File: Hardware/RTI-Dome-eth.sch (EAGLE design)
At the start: 79 parts, among them IC1 24AA128ST, IC3 FT232RL, IC5 74LVC245, IC6 74ABT245, J1 POWERPOLE_POWER45A, U1 W5500, X13 PN61729-S, X9 J1011F21PNL

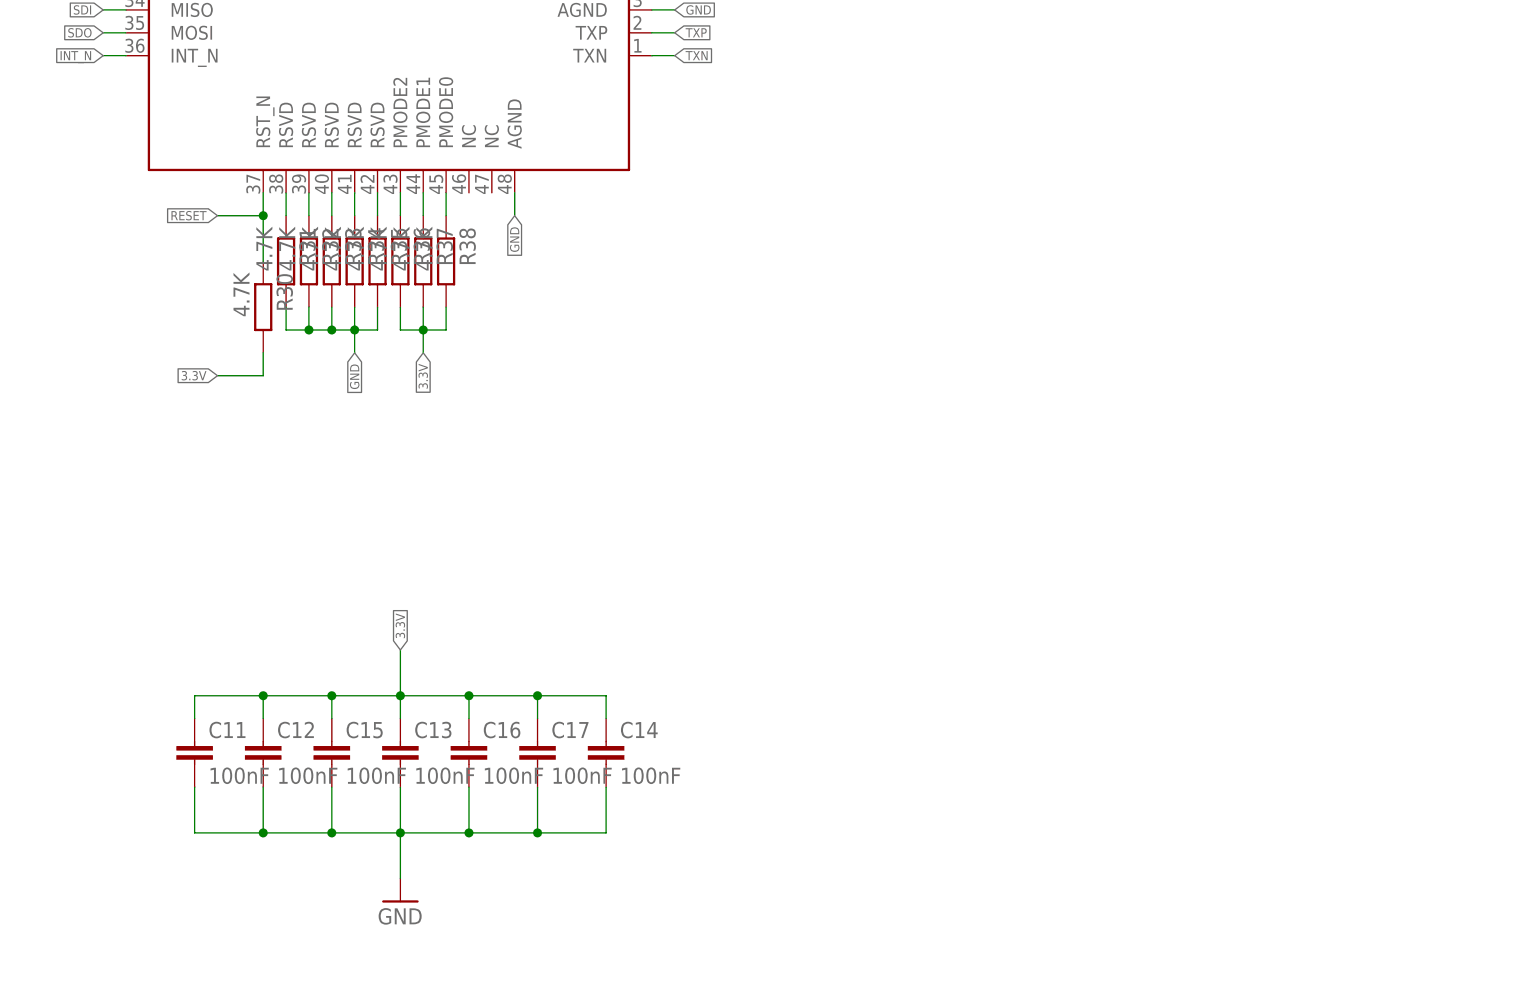
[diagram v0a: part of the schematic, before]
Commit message: Started routing the W5500
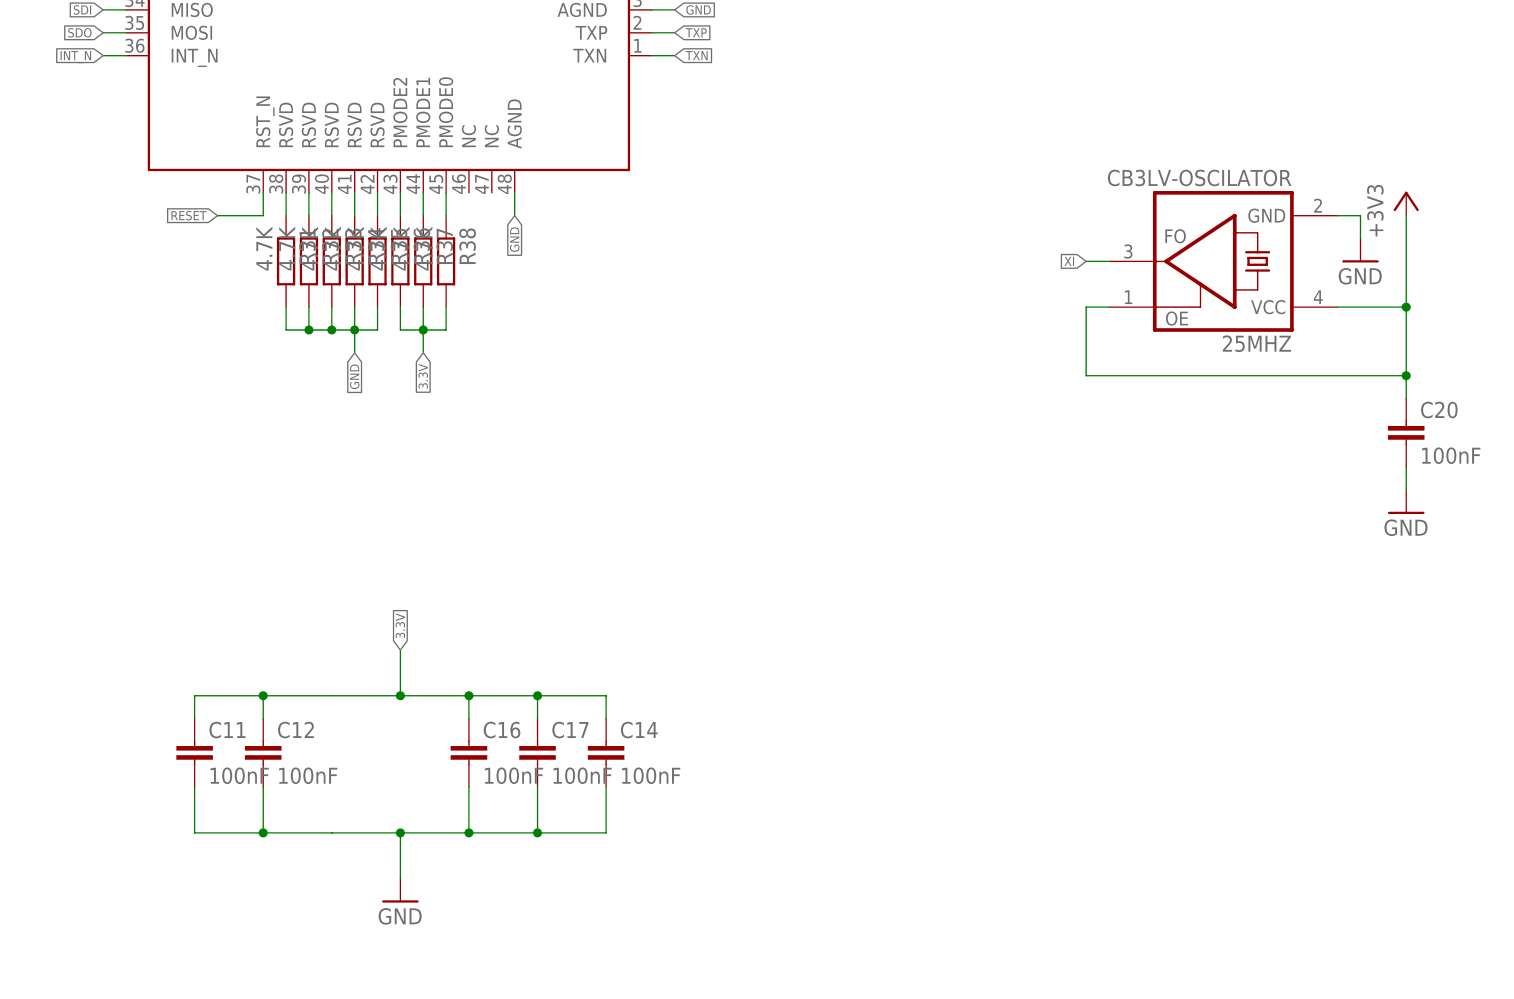
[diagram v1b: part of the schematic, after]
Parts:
- removed C13, C15: 100nF, rti:C-EU'0805'
- removed R30: 4.7K, rti:R-EU'0805'
- added 25MHZ: CB3LV-OSCILATOR, rti:CB3LV-OSCILATOR
- added C20: 100nF, rti:C-EU'0805'
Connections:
- new net +3V3: 25MHZ.OE, 25MHZ.VDD, C20.1
- net 3.3V: no longer C13.1, C15.1, R30.2
- net GND: now also 25MHZ.GND, C20.2; no longer C13.2, C15.2
- net RESET: no longer R30.1
- net XI: now also 25MHZ.FO
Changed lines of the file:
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@@
 <part name="X9" library="rti" deviceset="J1011F" device="" technology="21PNL" value="J1011F21PNL"/>
 <part name="GND16" library="supply1" deviceset="GND" device=""/>
-<part name="R30" library="rti" deviceset="R-EU" device="'0805'" value="4.7K"/>
 <part name="R31" library="rti" deviceset="R-EU" device="'0805'" value="4.7K"/>
 <part name="R32" library="rti" deviceset="R-EU" device="'0805'" value="4.7K"/>
@@
 <part name="C11" library="rti" deviceset="C-EU" device="'0805'" value="100nF"/>
 <part name="C12" library="rti" deviceset="C-EU" device="'0805'" value="100nF"/>
-<part name="C13" library="rti" deviceset="C-EU" device="'0805'" value="100nF"/>
 <part name="C14" library="rti" deviceset="C-EU" device="'0805'" value="100nF"/>
-<part name="C15" library="rti" deviceset="C-EU" device="'0805'" value="100nF"/>
 <part name="C16" library="rti" deviceset="C-EU" device="'0805'" value="100nF"/>
 <part name="C17" library="rti" deviceset="C-EU" device="'0805'" value="100nF"/>
@@
 <part name="R40" library="rti" deviceset="R-EU" device="'0805'" value="4.7K"/>
 <part name="J1" library="powerpoles" deviceset="POWERPOLE_POWER" device="45A"/>
+<part name="GND15" library="supply1" deviceset="GND" device=""/>
+<part name="25MHZ" library="rti" deviceset="CB3LV-OSCILATOR" device=""/>
+<part name="+3V15" library="supply1" deviceset="+3V3" device=""/>
+<part name="C20" library="rti" deviceset="C-EU" device="'0805'" value="100nF"/>
+<part name="GND17" library="supply1" deviceset="GND" device=""/>
 </parts>
 <sheets>
@@
 <instance part="X9" gate="G$1" x="568.96" y="269.24"/>
 <instance part="GND16" gate="1" x="548.64" y="233.68"/>
-<instance part="R30" gate="G$1" x="469.9" y="127" rot="R270"/>
 <instance part="R31" gate="G$1" x="472.44" y="132.08" rot="R270"/>
 <instance part="R32" gate="G$1" x="474.98" y="132.08" rot="R270"/>
@@
 <instance part="C11" gate="G$1" x="462.28" y="78.74"/>
 <instance part="C12" gate="G$1" x="469.9" y="78.74"/>
-<instance part="C13" gate="G$1" x="485.14" y="78.74"/>
 <instance part="C14" gate="G$1" x="508" y="78.74"/>
-<instance part="C15" gate="G$1" x="477.52" y="78.74"/>
 <instance part="C16" gate="G$1" x="492.76" y="78.74"/>
 <instance part="C17" gate="G$1" x="500.38" y="78.74"/>
@@
 <instance part="R40" gate="G$1" x="472.44" y="205.74" rot="R270"/>
 <instance part="J1" gate="G$1" x="378.46" y="83.82"/>
+<instance part="GND15" gate="1" x="591.82" y="132.08"/>
+<instance part="25MHZ" gate="G$1" x="576.58" y="132.08" rot="R180"/>
+<instance part="+3V15" gate="G$1" x="596.9" y="139.7"/>
+<instance part="C20" gate="G$1" x="596.9" y="114.3"/>
+<instance part="GND17" gate="1" x="596.9" y="104.14"/>
 </instances>
 <busses>
@@
 <wire x1="492.76" y1="73.66" x2="492.76" y2="68.58" width="0.1524" layer="91"/>
 <junction x="492.76" y="68.58"/>
-<pinref part="C13" gate="G$1" pin="2"/>
-<wire x1="485.14" y1="73.66" x2="485.14" y2="68.58" width="0.1524" layer="91"/>
 <junction x="485.14" y="68.58"/>
-<pinref part="C15" gate="G$1" pin="2"/>
-<wire x1="477.52" y1="73.66" x2="477.52" y2="68.58" width="0.1524" layer="91"/>
-<junction x="477.52" y="68.58"/>
 <pinref part="C12" gate="G$1" pin="2"/>
 <wire x1="469.9" y1="73.66" x2="469.9" y2="68.58" width="0.1524" layer="91"/>
@@
 <wire x1="472.44" y1="213.36" x2="472.44" y2="210.82" width="0.1524" layer="91"/>
 <label x="469.9" y="213.36" size="1.016" layer="95" rot="R180" xref="yes"/>
+</segment>
+<segment>
+<wire x1="589.28" y1="137.16" x2="591.82" y2="137.16" width="0.1524" layer="91"/>
+<wire x1="591.82" y1="137.16" x2="591.82" y2="134.62" width="0.1524" layer="91"/>
+<pinref part="GND15" gate="1" pin="GND"/>
+<pinref part="25MHZ" gate="G$1" pin="GND"/>
+</segment>
+<segment>
+<pinref part="C20" gate="G$1" pin="2"/>
+<wire x1="596.9" y1="106.68" x2="596.9" y2="109.22" width="0.1524" layer="91"/>
+<pinref part="GND17" gate="1" pin="GND"/>
 </segment>
 </net>
@@
 <wire x1="469.9" y1="81.28" x2="469.9" y2="83.82" width="0.1524" layer="91"/>
 <junction x="469.9" y="83.82"/>
-<pinref part="C15" gate="G$1" pin="1"/>
-<wire x1="477.52" y1="81.28" x2="477.52" y2="83.82" width="0.1524" layer="91"/>
-<junction x="477.52" y="83.82"/>
-<pinref part="C13" gate="G$1" pin="1"/>
-<wire x1="485.14" y1="81.28" x2="485.14" y2="83.82" width="0.1524" layer="91"/>
 <junction x="485.14" y="83.82"/>
 <pinref part="C16" gate="G$1" pin="1"/>
@@
 <wire x1="487.68" y1="124.46" x2="487.68" y2="121.92" width="0.1524" layer="91"/>
 <label x="487.68" y="121.92" size="1.016" layer="95" rot="R270" xref="yes"/>
-</segment>
-<segment>
-<pinref part="R30" gate="G$1" pin="2"/>
-<wire x1="469.9" y1="121.92" x2="469.9" y2="119.38" width="0.1524" layer="91"/>
-<wire x1="469.9" y1="119.38" x2="464.82" y2="119.38" width="0.1524" layer="91"/>
-<label x="464.82" y="119.38" size="1.016" layer="95" rot="R180" xref="yes"/>
 </segment>
 </net>
@@
 <label x="452.12" y="170.18" size="1.016" layer="95" rot="R180" xref="yes"/>
 </segment>
+<segment>
+<wire x1="563.88" y1="132.08" x2="561.34" y2="132.08" width="0.1524" layer="91"/>
+<pinref part="25MHZ" gate="G$1" pin="FO"/>
+<label x="561.34" y="132.08" size="1.016" layer="95" rot="R180" xref="yes"/>
+</segment>
 </net>
 <net name="XO" class="0">
@@
 <segment>
 <pinref part="U1" gate="G$1" pin="RST_N"/>
-<wire x1="469.9" y1="132.08" x2="469.9" y2="137.16" width="0.1524" layer="91"/>
-<pinref part="R30" gate="G$1" pin="1"/>
 <wire x1="469.9" y1="137.16" x2="469.9" y2="139.7" width="0.1524" layer="91"/>
 <wire x1="469.9" y1="137.16" x2="464.82" y2="137.16" width="0.1524" layer="91"/>
-<junction x="469.9" y="137.16"/>
 <label x="464.82" y="137.16" size="1.016" layer="95" rot="R180" xref="yes"/>
 </segment>
@@
 </segment>
 </net>
+<net name="+3V3" class="3">
+<segment>
+<wire x1="589.28" y1="127" x2="596.9" y2="127" width="0.1524" layer="91"/>
+<wire x1="596.9" y1="127" x2="596.9" y2="137.16" width="0.1524" layer="91"/>
+<wire x1="596.9" y1="119.38" x2="596.9" y2="127" width="0.1524" layer="91"/>
+<junction x="596.9" y="127"/>
+<pinref part="+3V15" gate="G$1" pin="+3V3"/>
+<pinref part="25MHZ" gate="G$1" pin="VDD"/>
+<pinref part="25MHZ" gate="G$1" pin="OE"/>
+<wire x1="563.88" y1="127" x2="561.34" y2="127" width="0.1524" layer="91"/>
+<wire x1="561.34" y1="127" x2="561.34" y2="119.38" width="0.1524" layer="91"/>
+<wire x1="561.34" y1="119.38" x2="596.9" y2="119.38" width="0.1524" layer="91"/>
+<pinref part="C20" gate="G$1" pin="1"/>
+<wire x1="596.9" y1="119.38" x2="596.9" y2="116.84" width="0.1524" layer="91"/>
+<junction x="596.9" y="119.38"/>
+</segment>
+</net>

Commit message: Added proper ethernet chip reset.
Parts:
- removed X12: (no value), con-ptr500:AK500/2
- added R30: 4.7K, rti:R-EU'0805'
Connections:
- removed net +3V3: 25MHZ.OE, 25MHZ.VDD, C20.1
- removed net RESET: U$1.RESET., U1.RST_N
- new net ETH_RESET: R30.1, U$1.53, U1.RST_N
- net 3.3V: now also 25MHZ.OE, 25MHZ.VDD, C20.1, R30.2
- net GND: now also U$1.GND@2, U$1.GND@3, U$1.GND@4, U$1.GND@5, U$1.GND@6; no longer U$1.GND., U$1.GND.., U$1.GND..., U$1.GND...., U$1.GND__, X12-1.KL, X12-2.KL
- net INT_N: now also U$1.32
- net VCC: now also U$1.+5V@3, U$1.+5V@4; no longer U$1.+5V., U$1.+5V..
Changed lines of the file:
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@@
 <part name="R3" library="rti" deviceset="R-EU" device="'0805'" value="1K"/>
 <part name="C5" library="rti" deviceset="C-EU" device="'0805'" value="100nF"/>
-<part name="X12" library="con-ptr500" deviceset="AK500/2" device=""/>
 <part name="IC3" library="ftdichip" deviceset="FT232R" device="L"/>
 <part name="GND10" library="supply1" deviceset="GND" device=""/>
@@
 <part name="GND15" library="supply1" deviceset="GND" device=""/>
 <part name="25MHZ" library="rti" deviceset="CB3LV-OSCILATOR" device=""/>
-<part name="+3V15" library="supply1" deviceset="+3V3" device=""/>
 <part name="C20" library="rti" deviceset="C-EU" device="'0805'" value="100nF"/>
 <part name="GND17" library="supply1" deviceset="GND" device=""/>
+<part name="R30" library="rti" deviceset="R-EU" device="'0805'" value="4.7K"/>
 </parts>
 <sheets>
@@
 <instance part="R3" gate="G$1" x="40.64" y="248.92" rot="R90"/>
 <instance part="C5" gate="G$1" x="114.3" y="180.34"/>
-<instance part="X12" gate="-1" x="378.46" y="129.54" rot="R180"/>
-<instance part="X12" gate="-2" x="378.46" y="134.62" rot="R180"/>
 <instance part="IC3" gate="1" x="289.56" y="149.86"/>
 <instance part="GND10" gate="1" x="274.32" y="111.76"/>
@@
 <instance part="GND15" gate="1" x="591.82" y="132.08"/>
 <instance part="25MHZ" gate="G$1" x="576.58" y="132.08" rot="R180"/>
-<instance part="+3V15" gate="G$1" x="596.9" y="139.7"/>
 <instance part="C20" gate="G$1" x="596.9" y="114.3"/>
 <instance part="GND17" gate="1" x="596.9" y="104.14"/>
+<instance part="R30" gate="G$1" x="469.9" y="129.54" rot="R270"/>
 </instances>
 <busses>
@@
 <wire x1="93.98" y1="106.68" x2="93.98" y2="104.14" width="0.1524" layer="91"/>
 <junction x="93.98" y="104.14"/>
-<pinref part="U$1" gate="G$1" pin="GND."/>
-<pinref part="U$1" gate="G$1" pin="GND.."/>
+<pinref part="U$1" gate="G$1" pin="GND@2"/>
+<pinref part="U$1" gate="G$1" pin="GND@3"/>
 </segment>
 <segment>
@@
 </segment>
 <segment>
-<pinref part="X12" gate="-1" pin="KL"/>
-<wire x1="370.84" y1="129.54" x2="373.38" y2="129.54" width="0.1524" layer="91"/>
-<label x="370.84" y="129.54" size="1.016" layer="95" rot="R180" xref="yes"/>
-</segment>
-<segment>
 <wire x1="116.84" y1="243.84" x2="119.38" y2="243.84" width="0.1524" layer="91"/>
 <label x="116.84" y="243.84" size="0.8128" layer="95" rot="R180" xref="yes"/>
@@
 <label x="187.96" y="238.76" size="0.8128" layer="95" rot="R180" xref="yes"/>
 <pinref part="IC6" gate="G$1" pin="A7"/>
-</segment>
-<segment>
-<pinref part="X12" gate="-2" pin="KL"/>
-<wire x1="370.84" y1="134.62" x2="373.38" y2="134.62" width="0.1524" layer="91"/>
-<label x="370.84" y="134.62" size="1.016" layer="95" rot="R180" xref="yes"/>
 </segment>
 <segment>
@@
 </segment>
 <segment>
-<pinref part="U$1" gate="G$1" pin="GND__"/>
+<pinref part="U$1" gate="G$1" pin="GND@6"/>
 <wire x1="127" y1="63.5" x2="129.54" y2="63.5" width="0.1524" layer="91"/>
 <label x="127" y="63.5" size="1.016" layer="95" rot="R180" xref="yes"/>
 </segment>
 <segment>
-<pinref part="U$1" gate="G$1" pin="GND...."/>
+<pinref part="U$1" gate="G$1" pin="GND@5"/>
 <wire x1="109.22" y1="20.32" x2="109.22" y2="17.78" width="0.1524" layer="91"/>
 <pinref part="GND9" gate="1" pin="GND"/>
-<pinref part="U$1" gate="G$1" pin="GND..."/>
+<pinref part="U$1" gate="G$1" pin="GND@4"/>
 <wire x1="109.22" y1="17.78" x2="109.22" y2="12.7" width="0.1524" layer="91"/>
 <wire x1="106.68" y1="45.72" x2="109.22" y2="45.72" width="0.1524" layer="91"/>
@@
 <wire x1="487.68" y1="124.46" x2="487.68" y2="121.92" width="0.1524" layer="91"/>
 <label x="487.68" y="121.92" size="1.016" layer="95" rot="R270" xref="yes"/>
+</segment>
+<segment>
+<pinref part="R30" gate="G$1" pin="2"/>
+<wire x1="469.9" y1="121.92" x2="469.9" y2="124.46" width="0.1524" layer="91"/>
+<label x="469.9" y="121.92" size="1.016" layer="95" rot="R270" xref="yes"/>
+</segment>
+<segment>
+<pinref part="25MHZ" gate="G$1" pin="OE"/>
+<wire x1="563.88" y1="127" x2="561.34" y2="127" width="0.1524" layer="91"/>
+<wire x1="561.34" y1="127" x2="561.34" y2="119.38" width="0.1524" layer="91"/>
+<wire x1="561.34" y1="119.38" x2="596.9" y2="119.38" width="0.1524" layer="91"/>
+<wire x1="596.9" y1="119.38" x2="596.9" y2="127" width="0.1524" layer="91"/>
+<pinref part="25MHZ" gate="G$1" pin="VDD"/>
+<wire x1="596.9" y1="127" x2="589.28" y2="127" width="0.1524" layer="91"/>
+<pinref part="C20" gate="G$1" pin="1"/>
+<wire x1="596.9" y1="119.38" x2="596.9" y2="116.84" width="0.1524" layer="91"/>
+<junction x="596.9" y="119.38"/>
+<wire x1="596.9" y1="127" x2="599.44" y2="127" width="0.1524" layer="91"/>
+<junction x="596.9" y="127"/>
+<label x="599.44" y="127" size="1.016" layer="95" xref="yes"/>
 </segment>
 </net>
@@
 </segment>
 <segment>
-<pinref part="U$1" gate="G$1" pin="+5V."/>
+<pinref part="U$1" gate="G$1" pin="+5V@3"/>
 <wire x1="152.4" y1="45.72" x2="152.4" y2="43.18" width="0.1524" layer="91"/>
 <wire x1="152.4" y1="45.72" x2="154.94" y2="45.72" width="0.1524" layer="91"/>
 <wire x1="154.94" y1="45.72" x2="154.94" y2="30.48" width="0.1524" layer="91"/>
-<pinref part="U$1" gate="G$1" pin="+5V.."/>
+<pinref part="U$1" gate="G$1" pin="+5V@4"/>
 <wire x1="154.94" y1="30.48" x2="154.94" y2="15.24" width="0.1524" layer="91"/>
 <wire x1="152.4" y1="20.32" x2="152.4" y2="15.24" width="0.1524" layer="91"/>
@@
 <label x="452.12" y="154.94" size="1.016" layer="95" rot="R180" xref="yes"/>
 </segment>
+<segment>
+<pinref part="U$1" gate="G$1" pin="32"/>
+<wire x1="137.16" y1="45.72" x2="137.16" y2="43.18" width="0.1524" layer="91"/>
+<label x="137.16" y="45.72" size="1.016" layer="95" rot="R90" xref="yes"/>
+</segment>
 </net>
 <net name="N$17" class="0">
@@
 </segment>
 </net>
-<net name="RESET" class="0">
-<segment>
-<pinref part="U1" gate="G$1" pin="RST_N"/>
-<wire x1="469.9" y1="137.16" x2="469.9" y2="139.7" width="0.1524" layer="91"/>
-<wire x1="469.9" y1="137.16" x2="464.82" y2="137.16" width="0.1524" layer="91"/>
-<label x="464.82" y="137.16" size="1.016" layer="95" rot="R180" xref="yes"/>
-</segment>
-<segment>
-<pinref part="U$1" gate="G$1" pin="RESET."/>
-<wire x1="127" y1="71.12" x2="129.54" y2="71.12" width="0.1524" layer="91"/>
-<label x="127" y="71.12" size="1.016" layer="95" rot="R180" xref="yes"/>
-</segment>
-</net>
 <net name="N$22" class="0">
 <segment>
@@
 </segment>
 </net>
-<net name="+3V3" class="3">
-<segment>
-<wire x1="589.28" y1="127" x2="596.9" y2="127" width="0.1524" layer="91"/>
-<wire x1="596.9" y1="127" x2="596.9" y2="137.16" width="0.1524" layer="91"/>
-<wire x1="596.9" y1="119.38" x2="596.9" y2="127" width="0.1524" layer="91"/>
-<junction x="596.9" y="127"/>
-<pinref part="+3V15" gate="G$1" pin="+3V3"/>
-<pinref part="25MHZ" gate="G$1" pin="VDD"/>
-<pinref part="25MHZ" gate="G$1" pin="OE"/>
-<wire x1="563.88" y1="127" x2="561.34" y2="127" width="0.1524" layer="91"/>
-<wire x1="561.34" y1="127" x2="561.34" y2="119.38" width="0.1524" layer="91"/>
-<wire x1="561.34" y1="119.38" x2="596.9" y2="119.38" width="0.1524" layer="91"/>
-<pinref part="C20" gate="G$1" pin="1"/>
-<wire x1="596.9" y1="119.38" x2="596.9" y2="116.84" width="0.1524" layer="91"/>
-<junction x="596.9" y="119.38"/>
-</segment>
-</net>
+<net name="ETH_RESET" class="0">
+<segment>
+<wire x1="111.76" y1="12.7" x2="114.3" y2="12.7" width="0.1524" layer="91"/>
+<label x="114.3" y="12.7" size="1.016" layer="95" xref="yes"/>
+<pinref part="U$1" gate="G$1" pin="53"/>
+<wire x1="111.76" y1="12.7" x2="111.76" y2="20.32" width="0.1524" layer="91"/>
+</segment>
+<segment>
+<pinref part="U1" gate="G$1" pin="RST_N"/>
+<pinref part="R30" gate="G$1" pin="1"/>
+<wire x1="469.9" y1="139.7" x2="469.9" y2="137.16" width="0.1524" layer="91"/>
+<wire x1="469.9" y1="137.16" x2="469.9" y2="134.62" width="0.1524" layer="91"/>
+<wire x1="469.9" y1="137.16" x2="467.36" y2="137.16" width="0.1524" layer="91"/>
+<junction x="469.9" y="137.16"/>
+<label x="467.36" y="137.16" size="1.016" layer="95" rot="R180" xref="yes"/>
+</segment>
+</net>
